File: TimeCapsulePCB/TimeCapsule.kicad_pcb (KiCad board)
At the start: 2 copper layers, 50 x 70 mm, 56 parts, among them J1 USB_C_Receptacle_USB2.0_14P, Q1 Q_PMOS_GSD, Q2 Q_NMOS_GSD, Q3 Q_NMOS_GSD, Q4 Q_NMOS_GSD, SW1 SW_Push, SW2 SW_Push, U1 RP2040, U2 TPL5110, U3 AP2112K-3.3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

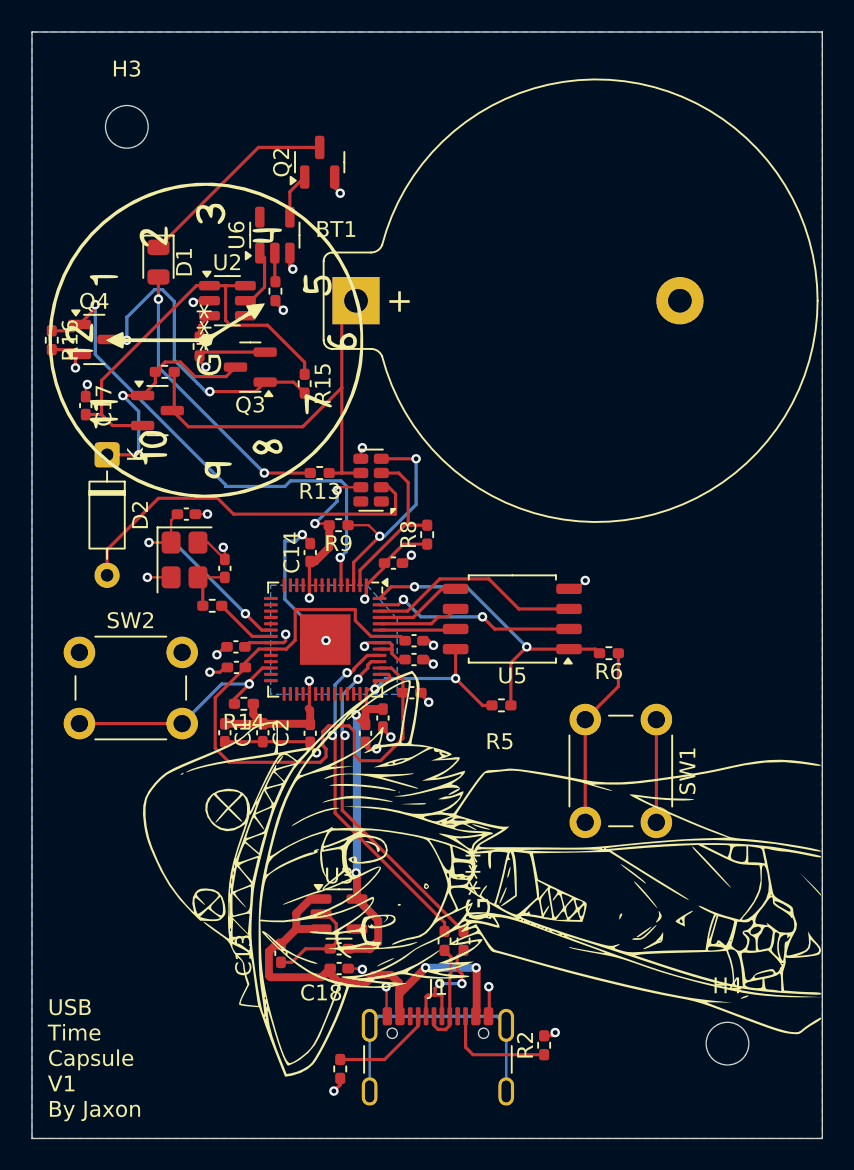
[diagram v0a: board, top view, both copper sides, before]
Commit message: Update readme and BOM
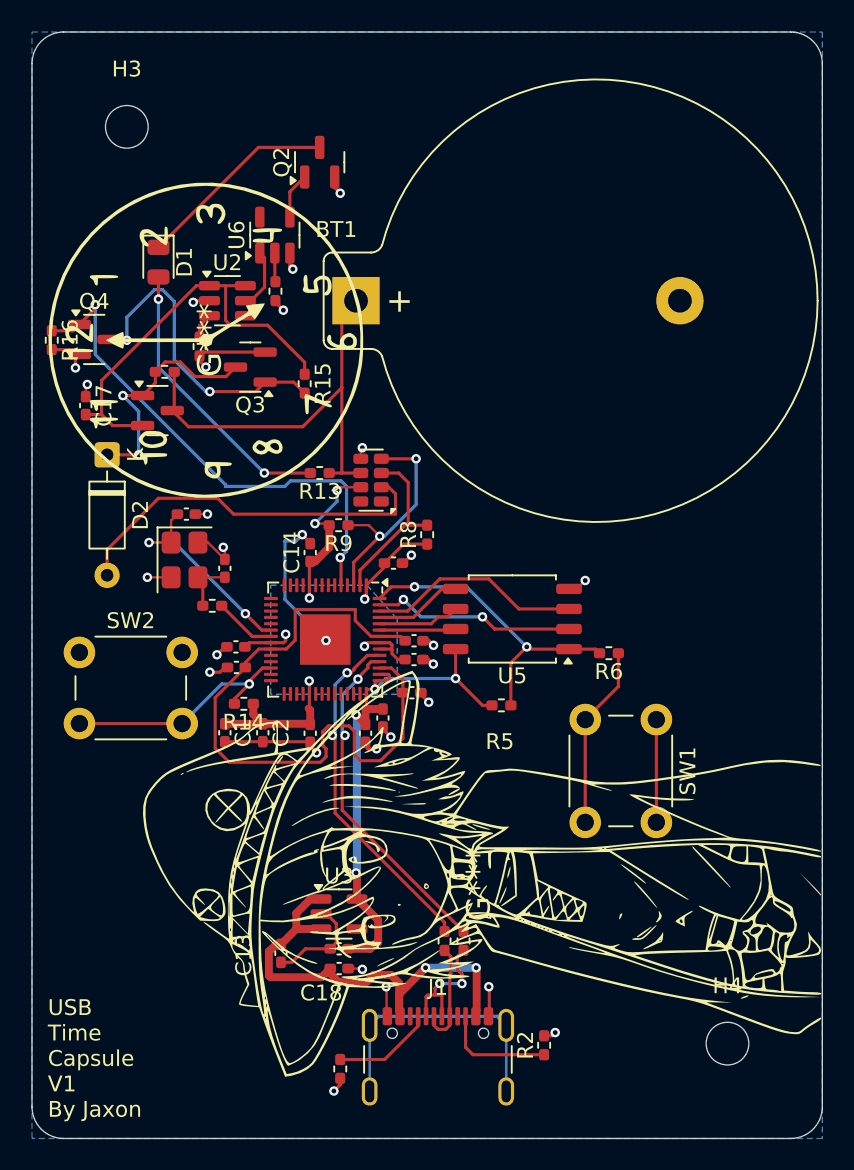
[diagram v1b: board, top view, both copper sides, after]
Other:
- outline, holes or cut-outs redrawn
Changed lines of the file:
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@@
 		(embedded_fonts no)
 	)
-	(gr_rect
-		(start 50 50)
-		(end 100 120)
+	(gr_arc
+		(start 52 120)
+		(mid 50.585786 119.414214)
+		(end 50 118)
 		(stroke
 			(width 0.05)
-			(type solid)
+			(type default)
 		)
-		(fill no)
 		(layer "Edge.Cuts")
 	)
+	(gr_arc
+		(start 100 118)
+		(mid 99.414214 119.414214)
+		(end 98 120)
+		(stroke
+			(width 0.05)
+			(type default)
+		)
+		(layer "Edge.Cuts")
+	)
+	(gr_line
+		(start 50 118)
+		(end 50 52)
+		(stroke
+			(width 0.05)
+			(type default)
+		)
+		(layer "Edge.Cuts")
+	)
+	(gr_arc
+		(start 50 52)
+		(mid 50.585786 50.585786)
+		(end 52 50)
+		(stroke
+			(width 0.05)
+			(type default)
+		)
+		(layer "Edge.Cuts")
+	)
+	(gr_line
+		(start 100 52)
+		(end 100 118)
+		(stroke
+			(width 0.05)
+			(type default)
+		)
+		(layer "Edge.Cuts")
+	)
+	(gr_line
+		(start 98 120)
+		(end 52 120)
+		(stroke
+			(width 0.05)
+			(type default)
+		)
+		(layer "Edge.Cuts")
+	)
+	(gr_line
+		(start 52 50)
+		(end 98 50)
+		(stroke
+			(width 0.05)
+			(type default)
+		)
+		(layer "Edge.Cuts")
+	)
+	(gr_arc
+		(start 98 50)
+		(mid 99.414214 50.585786)
+		(end 100 52)
+		(stroke
+			(width 0.05)
+			(type default)
+		)
+		(layer "Edge.Cuts")
+	)
